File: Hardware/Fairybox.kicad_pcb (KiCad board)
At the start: 2 copper layers, 91.4 x 55.9 mm, 72 parts, among them J1 REED, Q1 locked, Q10 locked, Q2 locked, Q3 locked, Q4 locked, Q5 locked, Q6 locked, Q7 locked, Q8 locked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

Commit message: Misc changes I forget
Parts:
- removed D8: locked, LED_THT:LED_D3.0mm-3
- added D22: LED_handsolder, Diode_SMD:D_1206_3216Metric_Pad1.42x1.75mm_HandSolder, F.Cu at (126.0, 89.0)
- added D23: LED_nominal, Diode_SMD:D_1206_3216Metric, F.Cu at (128.9, 88.9)
- TP6, TP7: value TP -> TestPoint_Small
- TP9: value tp -> TestPoint_Small
- moved R6 5.08 mm to (53.3, 95.9), turned to 90 degrees
- moved D21 4.83 mm to (131.6, 88.9)
- moved D2 3.30 mm to (139.5, 88.9)
- moved D18 0.77 mm to (111.4, 90.3)
- moved D19 0.77 mm to (117.6, 89.0)
- moved D20 0.77 mm to (120.7, 89.0)
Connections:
- net -BATT renamed CHARGE BOARD OUT B-
- net /MCU GPIO0 MOSI renamed MCU GPIO0 MOSI
- net /MCU GPIO1 MISO renamed MCU GPIO1 MISO
- net /MCU GPIO2 SCK renamed MCU GPIO2 SCK
- net /MCU GPIO3 renamed MCU GPIO3
- net /MCU GPIO4 renamed MCU GPIO4
- net /RP8 renamed /R7_AN
- net /SPI RST renamed Net-(R5-Pad1)
- BAT1 pad 1: /B+ -> /LI-ION_NEG
- BAT1 pad 2: /B- -> /LI-ION_NEG
- CC3 pad 1: +BATT -> /REED_RETURN
- J1 pad 1: +BATT -> CHARGE BOARD OUT B+
- R13 pad 2: /D8_AN2 -> /D23_AN
- R14 pad 2: /D8_AN1 -> /D22_AN
- R6 pad 1: /Q1_BASE -> /REED_RETURN
- R6 pad 2: /REED_RETURN -> /Q1_BASE
- U2 pad 1: +BATT -> CHARGE BOARD OUT B+
- UM1 pad 3: +BATT -> CHARGE BOARD OUT B+
- UM1 pad 5: /B+ -> /LI-ION_NEG
- UM1 pad 6: /B- -> /LI-ION_NEG
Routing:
- net /LI-ION_NEG: track 0.00 -> 100.4 mm
- net /B-: track 85.7 -> 0.00 mm
- net +BATT: track 53.3 -> 0.00 mm, vias 2 -> 0
- net CHARGE BOARD OUT B+: track 0.00 -> 46.3 mm, vias 0 -> 2
- net /B+: track 14.7 -> 0.00 mm
- net /Q8_COL: track 23.0 -> 36.7 mm
- net /REED_RETURN: track 7.40 -> 15.5 mm
- net /D8_AN1: track 7.60 -> 0.00 mm
- net /D22_AN: track 0.00 -> 7.60 mm
- net /D8_AN2: track 4.96 -> 0.00 mm
- net /D23_AN: track 0.00 -> 4.96 mm
- net /D21_AN: track 11.6 -> 8.26 mm
- net /D2_AN: track 12.4 -> 10.0 mm
- net MCU GPIO0 MOSI: track 39.0 -> 37.4 mm
- net /Q9_COL: track 32.9 -> 34.3 mm

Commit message: Update Fairybox.kicad_pcb
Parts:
- removed CC3: locked, Capacitor_THT:C_Disc_D3.0mm_W2.0mm_P2.50mm
- removed DI1: 1N914, Diode_THT:D_DO-35_SOD27_P7.62mm_Horizontal
- removed DI2: locked, Diode_THT:D_DO-35_SOD27_P7.62mm_Horizontal
- removed R18, R19, R7: locked, Resistor_THT:R_Axial_DIN0204_L3.6mm_D1.6mm_P5.08mm_Horizontal
- added D24: BLUE, Diode_SMD:D_1206_3216Metric, F.Cu at (62.9, 102.1)
- added D25: RED, Diode_SMD:D_1206_3216Metric, F.Cu at (63.5, 89.9)
- added D9: BLUE, Diode_SMD:D_1206_3216Metric, F.Cu at (114.2, 82.6)
- D21: renamed from D22; value LED_handsolder -> BLUE
- D23: value LED_nominal -> RED
- R16: footprint Resistor_THT:R_Axial_DIN0204_L3.6mm_D1.6mm_P5.08mm_Horizontal -> Resistor_SMD:R_1206_3216Metric
- R6: value locked -> 1K; footprint Resistor_THT:R_Axial_DIN0204_L3.6mm_D1.6mm_P5.08mm_Horizontal -> Resistor_SMD:R_1206_3216Metric
- R8: value 4.7K -> ??R; footprint Resistor_THT:R_Axial_DIN0204_L3.6mm_D1.6mm_P5.08mm_Horizontal -> Resistor_SMD:R_1206_3216Metric
- R9: value 47K -> ??R; footprint Resistor_THT:R_Axial_DIN0204_L3.6mm_D1.6mm_P5.08mm_Horizontal -> Resistor_SMD:R_1206_3216Metric
- TP10: value TestPoint_Small -> Q8_COL_TP
- TP11: value TestPoint_Small -> Q9_COL_TP
- TP12: value TestPoint_Small -> Q10_COL_TP
- TP6: value TestPoint_Small -> TPP
- TP7: value TestPoint_Small -> Q3_COL TP
- TP8: value TestPoint_Small -> Q2_TP
- TP9: value TestPoint_Small -> Q5_COL TP
- moved JP8 88.2 mm to (126.7, 98.6)
- moved R16 74.0 mm to (63.6, 85.2)
- moved JP2 37.9 mm to (77.6, 98.4)
- moved R8 31.9 mm to (62.9, 104.8), turned to 0 degrees
- moved JP1 28.9 mm to (78.6, 77.1)
- moved R9 26.9 mm to (114.1, 77.5), turned to -90 degrees
- moved JP7 24.5 mm to (136.8, 98.7)
- moved JP5 22.8 mm to (76.8, 74.5)
- moved R6 19.0 mm to (52.6, 76.9)
- moved JP6 17.9 mm to (85.3, 98.5)
- moved JP4 16.3 mm to (121.4, 98.7)
- moved JP3 16.2 mm to (49.7, 85.8)
- moved JP9 16.2 mm to (47.4, 81.9)
- moved TP1 14.6 mm to (91.4, 76.2)
- moved TP8 8.21 mm to (67.1, 98.6)
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- renumbered D21 to D22
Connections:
- net /D7_AN renamed Net-(D4-Pad1)
- net /Q3_COL renamed /D6_AN
- net CHARGE BOARD OUT B+ renamed /CHARGE BOARD OUT B+
- net CHARGE BOARD OUT B- renamed /CHARGE BOARD OUT B-
- net MCU GPIO0 MOSI renamed /MCU GPIO0 MOSI
- net MCU GPIO1 MISO renamed /MCU GPIO1 MISO
- net MCU GPIO2 SCK renamed /MCU GPIO2 SCK
- net Net-(R5-Pad1) renamed /MCU RST
- BAT1 pad 1: /LI-ION_NEG -> /LI-ION_POS
- D21 pad 1: Net-(DI1-Pad2) -> /Q7_COL
- D23 pad 1: Net-(DI1-Pad2) -> /Q8_COL
- Q10 pad 3: MCU GPIO4 -> /MCU GPIO4
- Q2 pad 3: /Q2_BASE -> /MCU GPIO4
- Q3 pad 3: MCU GPIO4 -> /MCU GPIO4
- Q4 pad 3: MCU GPIO3 -> /MCU GPIO3
- Q5 pad 3: /Q5_BASE -> /MCU GPIO3
- R16 pad 2: /R17_AN -> /D25_AN
- R8 pad 1: MCU GPIO3 -> +5V
- R8 pad 2: /Q5_BASE -> /D24_AN
- R9 pad 1: MCU GPIO3 -> +5V
- R9 pad 2: GND -> /D9_AN
- U1 pad 2: MCU GPIO3 -> /MCU GPIO3
- U1 pad 3: MCU GPIO4 -> /MCU GPIO4
- UM1 pad 5: /LI-ION_NEG -> /LI-ION_POS
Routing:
- net MCU GPIO4: track 113.2 -> 0.00 mm
- net /MCU GPIO4: track 0.00 -> 111.4 mm
- net MCU GPIO3: track 38.4 -> 0.00 mm
- net /MCU GPIO3: track 0.00 -> 36.8 mm
- net Net-(DI1-Pad2): track 33.8 -> 0.00 mm, vias 2 -> 0
- net +5V: track 125.3 -> 155.4 mm
- net /Q1_BASE: track 29.4 -> 2.24 mm, vias 2 -> 0
- net /LI-ION_POS: track 0.00 -> 20.4 mm
- net /CHARGE BOARD OUT B-: track 31.2 -> 11.7 mm
- net /Q8_COL: track 36.7 -> 20.3 mm
- net /Q2_COL: track 9.49 -> 22.3 mm
- net /LI-ION_NEG: track 100.4 -> 88.9 mm
- net /REED_RETURN: track 15.5 -> 25.4 mm
- net /Q2_BASE: track 7.30 -> 0.00 mm
- net /Q9_COL: track 34.3 -> 28.2 mm
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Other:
- board text removed: "//"

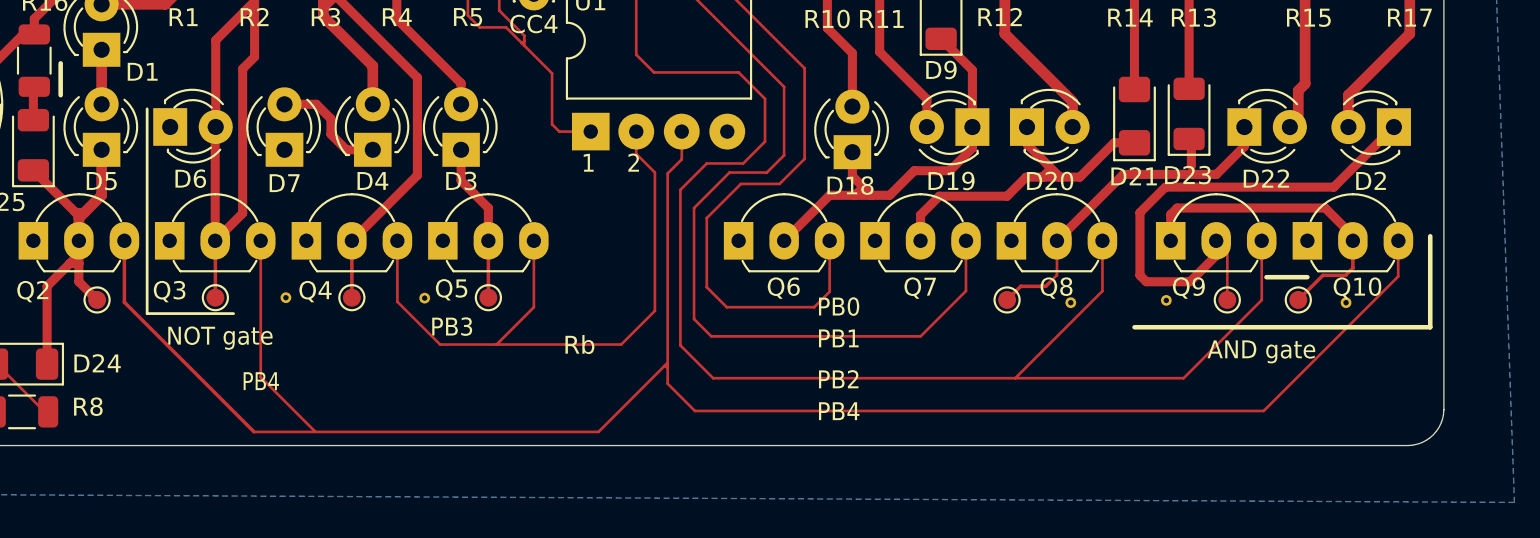
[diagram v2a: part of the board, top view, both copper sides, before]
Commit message: Updated testpoints and silkscreen
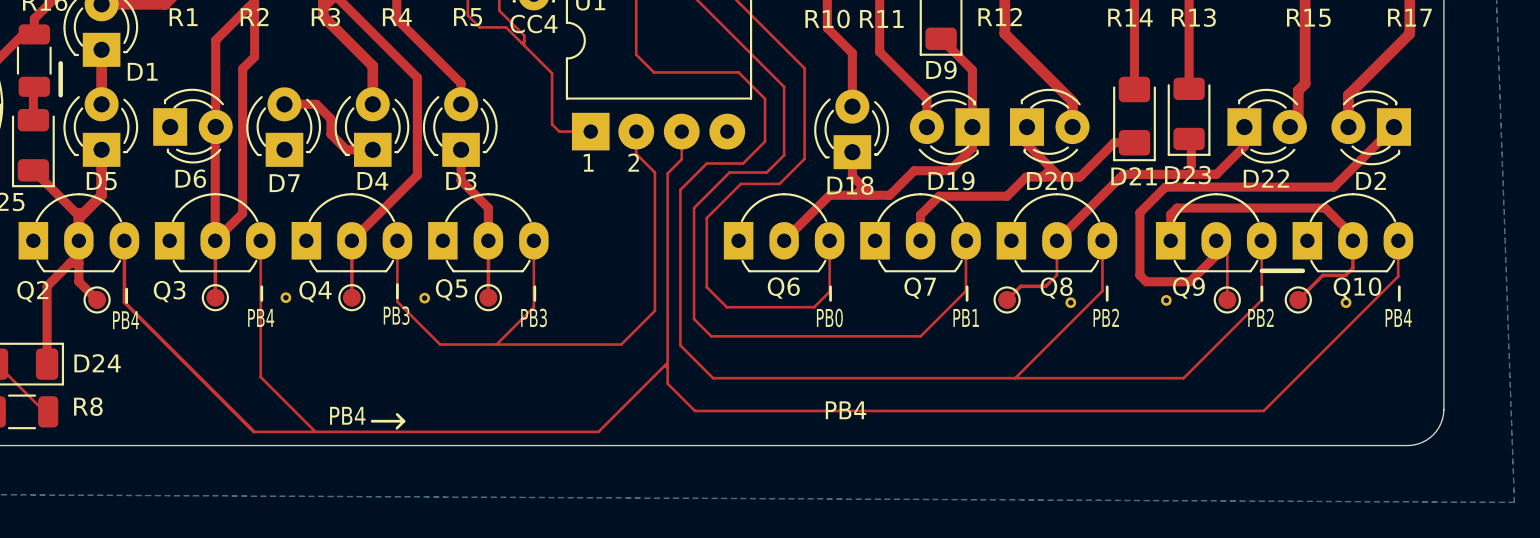
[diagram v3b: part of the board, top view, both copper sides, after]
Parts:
- JP2, JP4, JP6, JP7, JP8: footprint UltraLibrary:Via-GND -> UltraLibrary:PTH-Test_Point
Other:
- board text removed: "AND gate"
- board text removed: "NOT gate"
- board text removed: "Rb"
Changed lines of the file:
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@@
     )
   )
-  (footprint "UltraLibrary:Via-GND" (layer "F.Cu")
+  (footprint "UltraLibrary:PTH-Test_Point" (layer "F.Cu")
     (at 77.597 98.425)
     (property "Sheetfile" "Fairybox.kicad_sch")
@@
       (effects (font (size 1 1) (thickness 0.15)))
     )
-    (fp_text user "${REFERENCE}" (at 0 2.5 unlocked) (layer "F.Fab")
+    (fp_text user "${REFERENCE}" (at 0 1.143 unlocked) (layer "F.Fab") hide
       (effects (font (size 1 1) (thickness 0.15)))
     )
-    (pad "1" thru_hole circle (at 0 0) (size 0.6 0.6) (drill 0.3) (layers *.Cu *.Mask)
+    (pad "1" thru_hole circle (at 0 0) (size 0.6 0.6) (drill 0.3) (layers *.Cu "F.Mask")
       (net 1 "GND") (pinfunction "GND") (pintype "input") (zone_connect 2))
   )
@@
     )
   )
-  (footprint "UltraLibrary:Via-GND" (layer "F.Cu")
+  (footprint "UltraLibrary:PTH-Test_Point" (layer "F.Cu")
     (at 136.779 98.7044)
     (property "Sheetfile" "Fairybox.kicad_sch")
@@
     )
     (fp_text value "ViaGND" (at 0 1 unlocked) (layer "F.Fab") hide
-      (effects (font (size 0.8 0.8) (thickness 0.15)))
+      (effects (font (size 1 1) (thickness 0.15)))
     )
-    (fp_text user "${REFERENCE}" (at 1.524 7.62 unlocked) (layer "F.Fab") hide
+    (fp_text user "${REFERENCE}" (at 0 1.143 unlocked) (layer "F.Fab") hide
       (effects (font (size 1 1) (thickness 0.15)))
     )
-    (pad "1" thru_hole circle (at 0 0) (size 0.6 0.6) (drill 0.3) (layers *.Cu *.Mask)
+    (pad "1" thru_hole circle (at 0 0) (size 0.6 0.6) (drill 0.3) (layers *.Cu "F.Mask")
       (net 1 "GND") (pinfunction "GND") (pintype "input") (zone_connect 2))
   )
@@
     )
   )
-  (footprint "UltraLibrary:Via-GND" (layer "F.Cu")
+  (footprint "UltraLibrary:PTH-Test_Point" (layer "F.Cu")
     (at 85.344 98.4504)
     (property "Sheetfile" "Fairybox.kicad_sch")
@@
     )
     (fp_text value "ViaGND" (at 0 1 unlocked) (layer "F.Fab") hide
-      (effects (font (size 0.8 0.8) (thickness 0.15)))
+      (effects (font (size 1 1) (thickness 0.15)))
     )
-    (fp_text user "${REFERENCE}" (at -2.032 6.096 unlocked) (layer "F.Fab") hide
+    (fp_text user "${REFERENCE}" (at 0 1.143 unlocked) (layer "F.Fab") hide
       (effects (font (size 1 1) (thickness 0.15)))
     )
-    (pad "1" thru_hole circle (at 0 0) (size 0.6 0.6) (drill 0.3) (layers *.Cu *.Mask)
+    (pad "1" thru_hole circle (at 0 0) (size 0.6 0.6) (drill 0.3) (layers *.Cu "F.Mask")
       (net 1 "GND") (pinfunction "GND") (pintype "input") (zone_connect 2))
   )
@@
     )
   )
-  (footprint "UltraLibrary:Via-GND" (layer "F.Cu")
+  (footprint "UltraLibrary:PTH-Test_Point" (layer "F.Cu")
     (at 121.412 98.7044)
     (property "Sheetfile" "Fairybox.kicad_sch")
@@
     )
     (fp_text value "ViaGND" (at 0 1 unlocked) (layer "F.Fab") hide
-      (effects (font (size 0.8 0.8) (thickness 0.15)))
+      (effects (font (size 1 1) (thickness 0.15)))
     )
-    (fp_text user "${REFERENCE}" (at 0 2.5 unlocked) (layer "F.Fab") hide
+    (fp_text user "${REFERENCE}" (at 0 1.143 unlocked) (layer "F.Fab") hide
       (effects (font (size 1 1) (thickness 0.15)))
     )
-    (pad "1" thru_hole circle (at 0 0) (size 0.6 0.6) (drill 0.3) (layers *.Cu *.Mask)
+    (pad "1" thru_hole circle (at 0 0) (size 0.6 0.6) (drill 0.3) (layers *.Cu "F.Mask")
       (net 1 "GND") (pinfunction "GND") (pintype "input") (zone_connect 2))
   )
@@
       (net 37 "/D6_AN") (pinfunction "1") (pintype "passive"))
   )
-  (footprint "UltraLibrary:Via-GND" (layer "F.Cu")
+  (footprint "UltraLibrary:PTH-Test_Point" (layer "F.Cu")
     (at 126.746 98.5774)
     (property "Sheetfile" "Fairybox.kicad_sch")
@@
     )
     (fp_text value "ViaGND" (at 0 1 unlocked) (layer "F.Fab") hide
-      (effects (font (size 0.8 0.8) (thickness 0.15)))
+      (effects (font (size 1 1) (thickness 0.15)))
     )
-    (fp_text user "${REFERENCE}" (at 0 2.5 unlocked) (layer "F.Fab") hide
+    (fp_text user "${REFERENCE}" (at 0 1.143 unlocked) (layer "F.Fab") hide
       (effects (font (size 1 1) (thickness 0.15)))
     )
-    (pad "1" thru_hole circle (at 0 0) (size 0.6 0.6) (drill 0.3) (layers *.Cu *.Mask)
+    (pad "1" thru_hole circle (at 0 0) (size 0.6 0.6) (drill 0.3) (layers *.Cu "F.Mask")
       (net 1 "GND") (pinfunction "GND") (pintype "input") (zone_connect 2))
   )
@@
     )
   )
-  (gr_line (start 132.334 97.282) (end 134.62 97.282) (layer "F.SilkS") (width 0.254))
+  (gr_line (start 132.08 96.9264) (end 134.366 96.9264) (layer "F.SilkS") (width 0.254))
+  (gr_line (start 76.2508 98.5774) (end 76.2508 97.8154) (layer "F.SilkS") (width 0.153))
+  (gr_line (start 123.444 98.5774) (end 123.444 97.8154) (layer "F.SilkS") (width 0.153))
   (gr_line (start 65.024 85.344) (end 65.024 87.122) (layer "F.SilkS") (width 0.254))
-  (gr_line (start 124.968 100.076) (end 141.478 100.076) (layer "F.SilkS") (width 0.254))
-  (gr_line (start 69.85 99.314) (end 74.676 99.314) (layer "F.SilkS") (width 0.153))
-  (gr_line (start 69.85 99.314) (end 69.85 87.884) (layer "F.SilkS") (width 0.153))
-  (gr_line (start 141.478 100.076) (end 141.478 94.996) (layer "F.SilkS") (width 0.254))
+  (gr_line (start 83.8073 104.9401) (end 84.1883 105.3211) (layer "F.SilkS") (width 0.153))
+  (gr_line (start 82.4103 105.3211) (end 84.1883 105.3211) (layer "F.SilkS") (width 0.153))
+  (gr_line (start 91.4908 98.5774) (end 91.4908 97.8154) (layer "F.SilkS") (width 0.153))
+  (gr_line (start 115.6208 98.5774) (end 115.6208 97.8154) (layer "F.SilkS") (width 0.153))
+  (gr_line (start 139.7508 98.5774) (end 139.7508 97.8154) (layer "F.SilkS") (width 0.153))
+  (gr_line (start 108.0008 98.5774) (end 108.0008 97.8154) (layer "F.SilkS") (width 0.153))
   (gr_rect (start 216.154 -53.34) (end 213.614 -55.88) (layer "F.SilkS") (width 0.254) (fill none))
+  (gr_line (start 68.707 98.7044) (end 68.707 97.9424) (layer "F.SilkS") (width 0.153))
+  (gr_line (start 132.08 98.5774) (end 132.08 97.8154) (layer "F.SilkS") (width 0.153))
+  (gr_line (start 83.82 98.4504) (end 83.82 97.6884) (layer "F.SilkS") (width 0.153))
+  (gr_line (start 83.7946 105.7148) (end 84.1756 105.3338) (layer "F.SilkS") (width 0.153))
   (gr_line (start 142.24 104.68) (end 142.24 52.8) (layer "Edge.Cuts") (width 0.0381))
   (gr_arc (start 50.8 52.8) (mid 51.385786 51.385786) (end 52.8 50.8) (layer "Edge.Cuts") (width 0.0381))
@@
     (effects (font (size 1 0.93) (thickness 0.155)))
   )
+  (gr_text "PB4" (at 68.6562 99.7204) (layer "F.SilkS")
+    (effects (font (size 1 0.6) (thickness 0.15)))
+  )
   (gr_text "2" (at 97.028 90.932) (layer "F.SilkS")
     (effects (font (size 1 0.93) (thickness 0.155)))
   )
-  (gr_text "Rb" (at 93.98 101.092) (layer "F.SilkS")
-    (effects (font (size 1 1) (thickness 0.15)))
-  )
   (gr_text "5V" (at 48.5902 73.279) (layer "F.SilkS")
     (effects (font (size 1 0.8128) (thickness 0.153)))
   )
-  (gr_text "PB3" (at 86.868 100.076) (layer "F.SilkS")
-    (effects (font (size 1 0.93) (thickness 0.155)))
-  )
-  (gr_text "PB1" (at 108.458 100.7364) (layer "F.SilkS")
-    (effects (font (size 1 0.93) (thickness 0.155)))
+  (gr_text "PB3" (at 83.7692 99.4664) (layer "F.SilkS")
+    (effects (font (size 1 0.6) (thickness 0.15)))
   )
   (gr_text "B+" (at 59.182 105.918) (layer "F.SilkS")
@@
     (effects (font (size 1 0.93) (thickness 0.155)))
   )
-  (gr_text "AND gate" (at 132.08 101.346) (layer "F.SilkS")
-    (effects (font (size 1 0.93) (thickness 0.155)))
+  (gr_text "PB4" (at 76.2 99.5934) (layer "F.SilkS")
+    (effects (font (size 1 0.6) (thickness 0.15)))
   )
-  (gr_text "NOT gate" (at 73.914 100.584) (layer "F.SilkS")
-    (effects (font (size 1 0.93) (thickness 0.155)))
+  (gr_text "PB3" (at 91.44 99.5934) (layer "F.SilkS")
+    (effects (font (size 1 0.6) (thickness 0.15)))
   )
-  (gr_text "PB4" (at 108.458 104.8004) (layer "F.SilkS")
+  (gr_text "PB4" (at 108.839 104.7496) (layer "F.SilkS")
     (effects (font (size 1 0.93) (thickness 0.155)))
   )
@@
     (effects (font (size 1 0.93) (thickness 0.155)))
   )
-  (gr_text "PB2" (at 108.458 103.0224) (layer "F.SilkS")
-    (effects (font (size 1 0.93) (thickness 0.155)))
+  (gr_text "PB4" (at 139.7 99.5934) (layer "F.SilkS")
+    (effects (font (size 1 0.6) (thickness 0.15)))
+  )
+  (gr_text "PB2" (at 132.0292 99.5934) (layer "F.SilkS")
+    (effects (font (size 1 0.6) (thickness 0.15)))
+  )
+  (gr_text "PB2" (at 123.3932 99.5934) (layer "F.SilkS")
+    (effects (font (size 1 0.6) (thickness 0.15)))
   )
   (gr_text "B-" (at 54.991 105.791) (layer "F.SilkS")
     (effects (font (size 1 0.8128) (thickness 0.153)))
   )
-  (gr_text "PB4" (at 76.2 103.124) (layer "F.SilkS")
+  (gr_text "PB4" (at 81.026 105.0544) (layer "F.SilkS")
     (effects (font (size 1 0.8128) (thickness 0.153)))
   )
+  (gr_text "PB1" (at 115.57 99.5934) (layer "F.SilkS")
+    (effects (font (size 1 0.6) (thickness 0.15)))
+  )
   (gr_text "1" (at 57.0484 70.7136) (layer "F.SilkS")
     (effects (font (size 1 0.8128) (thickness 0.153)))
@@
     (effects (font (size 1 0.8128) (thickness 0.153)))
   )
-  (gr_text "PB0" (at 108.458 98.9584) (layer "F.SilkS")
-    (effects (font (size 1 0.93) (thickness 0.155)))
+  (gr_text "PB0" (at 107.95 99.5934) (layer "F.SilkS")
+    (effects (font (size 1 0.6) (thickness 0.15)))
   )
   (segment (start 54.102 87.620723) (end 54.102 81.4324) (width 0.508) (layer "F.Cu") (net 1))
@@
     )
   )
+  (group "" (id 19127f95-b3e8-4eb0-b9f9-76825b269b1a)
+    (members
+      49314b92-1f8e-48a7-b3b0-ef67f08d7d1f
+      684a8d97-44b4-4090-9326-90c0b2cd5ae5
+      fc6a739c-bfd5-4bd6-8b8e-ca54452243d3
+    )
+  )

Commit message: misc
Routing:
- net /MCU GPIO3: track 36.8 -> 33.6 mm
- net /MCU GPIO2 SCK: track 80.9 -> 83.4 mm
- net /MCU GPIO4: track 111.4 -> 113.5 mm
- net /MCU GPIO1 MISO: track 48.9 -> 50.9 mm
- net +5V: track 155.4 -> 156.3 mm
- net /Q8_COL: track 20.3 -> 21.2 mm
- net /CHARGE BOARD OUT B+: track 42.1 -> 41.3 mm
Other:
- board text added: "0"
- board text added: "10"
- board text added: "9"
- board text removed: "5"
